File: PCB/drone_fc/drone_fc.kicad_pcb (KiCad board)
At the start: 4 copper layers, 1 part, among them U1 nRF52840

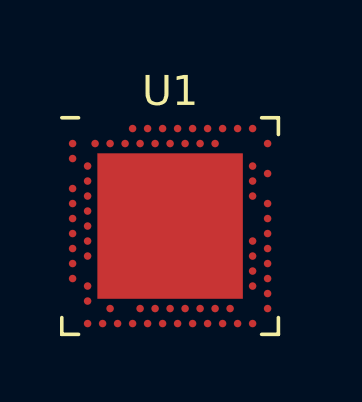
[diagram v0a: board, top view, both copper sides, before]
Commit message: Starting a PCB with the nRF52840. The Nordic-provided boards crash KiCAD so I'm making it myself I guess
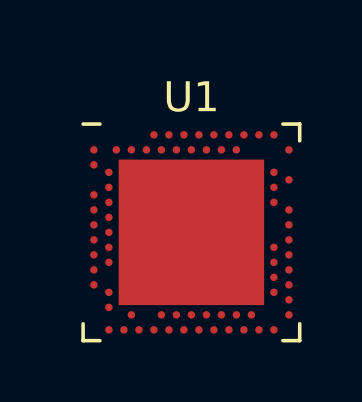
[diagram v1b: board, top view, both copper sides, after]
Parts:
- U1: footprint Package_DFN_QFN:Nordic_AQFN-73-1EP_7x7mm_P0.5mm -> nRF52840:nRF52840
- moved U1 0.74 mm to (53.3, 38.1)
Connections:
- U1 pad A22: Net-(U1-VDD-PadA22) -> unconnected-(U1-VDD-PadA22)
- U1 pad AD14: Net-(U1-VDD-PadA22) -> unconnected-(U1-VDD-PadAD14)
- U1 pad AD23: Net-(U1-VDD-PadA22) -> unconnected-(U1-VDD-PadAD23)
- U1 pad B1: Net-(U1-VDD-PadA22) -> VDD
- U1 pad B7: Net-(U1-VSS-PadB7) -> unconnected-(U1-VSS-PadB7)
- U1 pad W1: Net-(U1-VDD-PadA22) -> unconnected-(U1-VDD-PadW1)

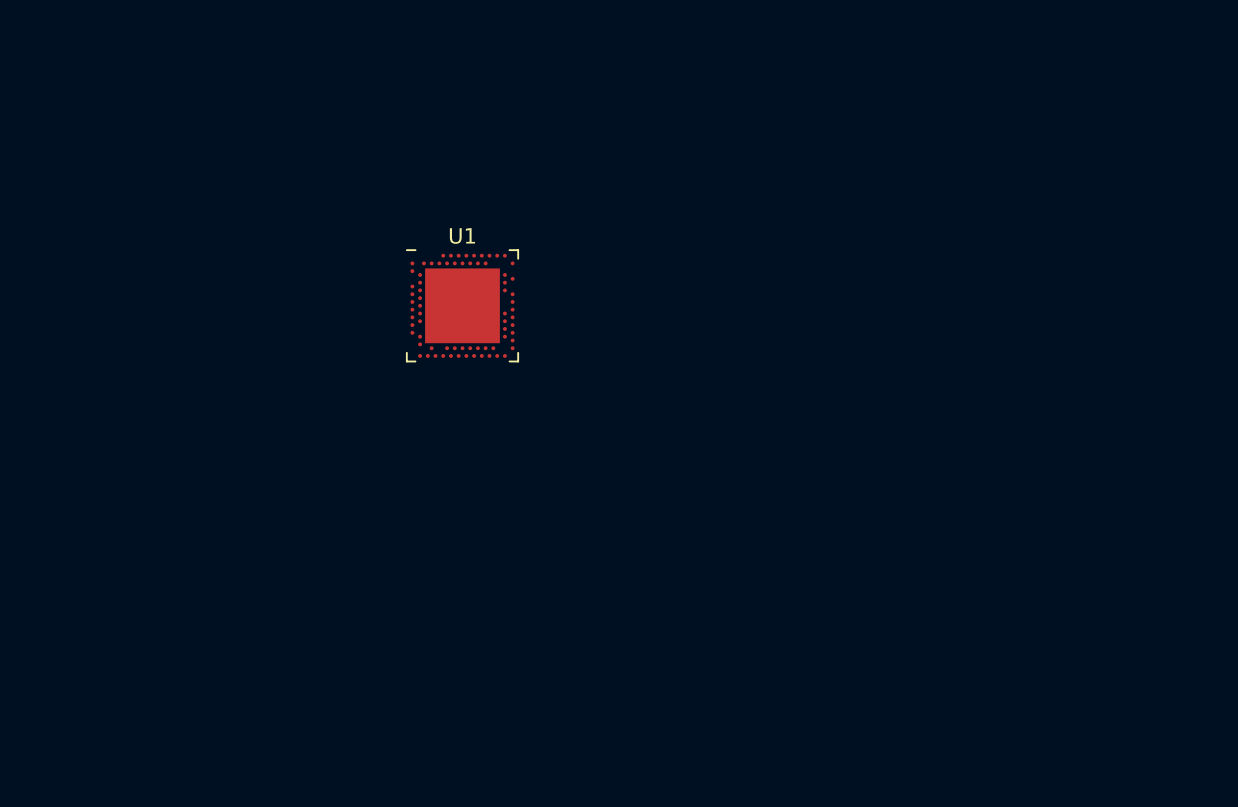
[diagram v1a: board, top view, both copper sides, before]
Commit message: Finished basic configuration schematic for nRF52840 and added USB receptacle and ESD protection
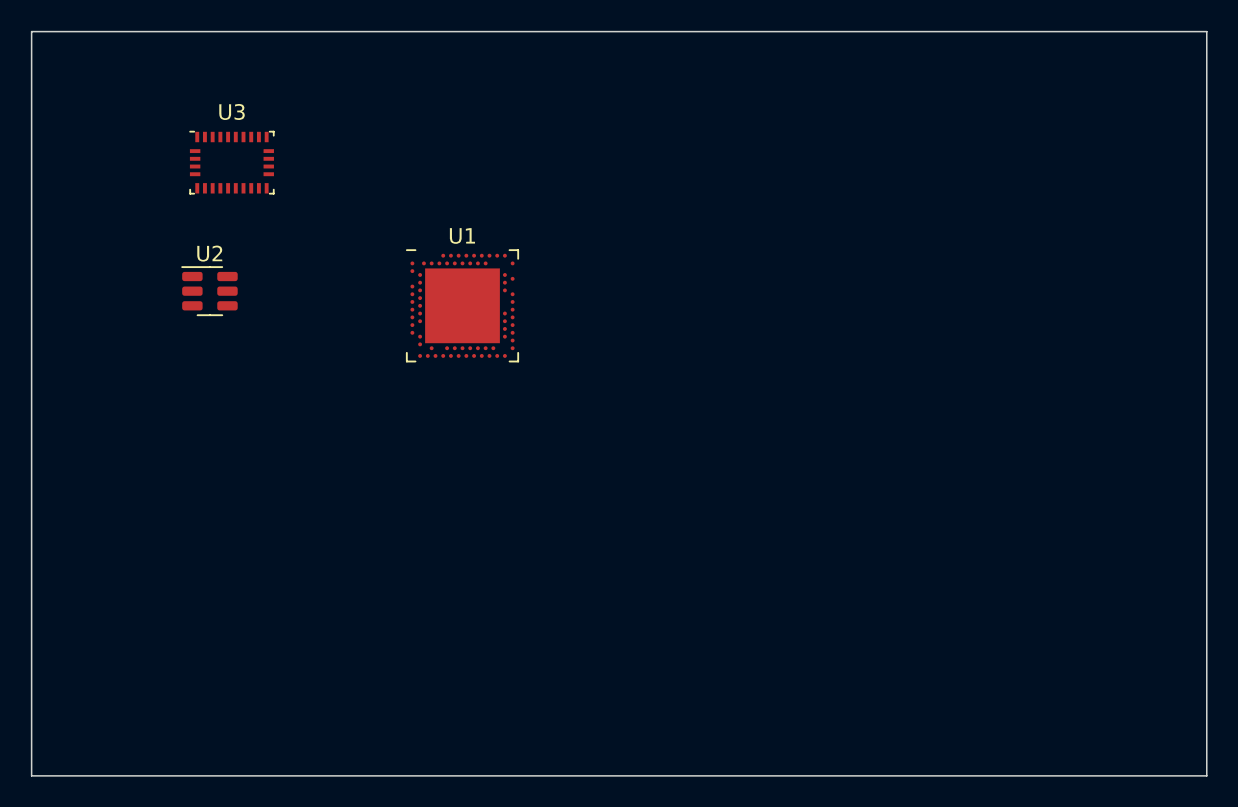
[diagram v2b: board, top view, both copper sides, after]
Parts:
- added U2: USBLC6-2SC6, Package_TO_SOT_SMD:SOT-23-6, F.Cu at (37.0, 37.1)
- added U3: BNO055, Package_LGA:LGA-28_5.2x3.8mm_P0.5mm, F.Cu at (38.4, 28.8)
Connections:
- U1 pad A18: unconnected-(U1-DEC2-PadA18) -> Net-(U1-DEC2)
- U1 pad A22: unconnected-(U1-VDD-PadA22) -> +15V
- U1 pad A23: unconnected-(U1-XC2-PadA23) -> Net-(U1-XC2)
- U1 pad AC5: unconnected-(U1-DECUSB-PadAC5) -> Net-(U1-DECUSB)
- U1 pad AD14: unconnected-(U1-VDD-PadAD14) -> +15V
- U1 pad AD2: unconnected-(U1-VBUS-PadAD2) -> VBUS
- U1 pad AD23: unconnected-(U1-VDD-PadAD23) -> +15V
- U1 pad AD4: unconnected-(U1-D--PadAD4) -> /D-
- U1 pad AD6: unconnected-(U1-D+-PadAD6) -> /D+
- U1 pad B1: VDD -> +15V
- U1 pad B24: unconnected-(U1-XC1-PadB24) -> Net-(U1-XC1)
- U1 pad B5: unconnected-(U1-DEC4-PadB5) -> /DEC4_6
- U1 pad B7: unconnected-(U1-VSS-PadB7) -> GND
- U1 pad C1: unconnected-(U1-DEC1-PadC1) -> /DEC1
- U1 pad D23: unconnected-(U1-DEC3-PadD23) -> /DEC3
- U1 pad E24: unconnected-(U1-DEC6-PadE24) -> /DEC4_6
- U1 pad F23: unconnected-(U1-VSS_PA-PadF23) -> GND
- U1 pad H23: unconnected-(U1-ANT-PadH23) -> Net-(U1-ANT)
- U1 pad W1: unconnected-(U1-VDD-PadW1) -> +15V
- U1 pad Y2: unconnected-(U1-VDDH-PadY2) -> VDDH
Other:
- board outline added: 76.2 x 48.3 mm

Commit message: Well the BNO055 isn't recommended for new projects, so I've replaced it with the ICM-20948, and updated the PCB's edge to hopefully match the ESC
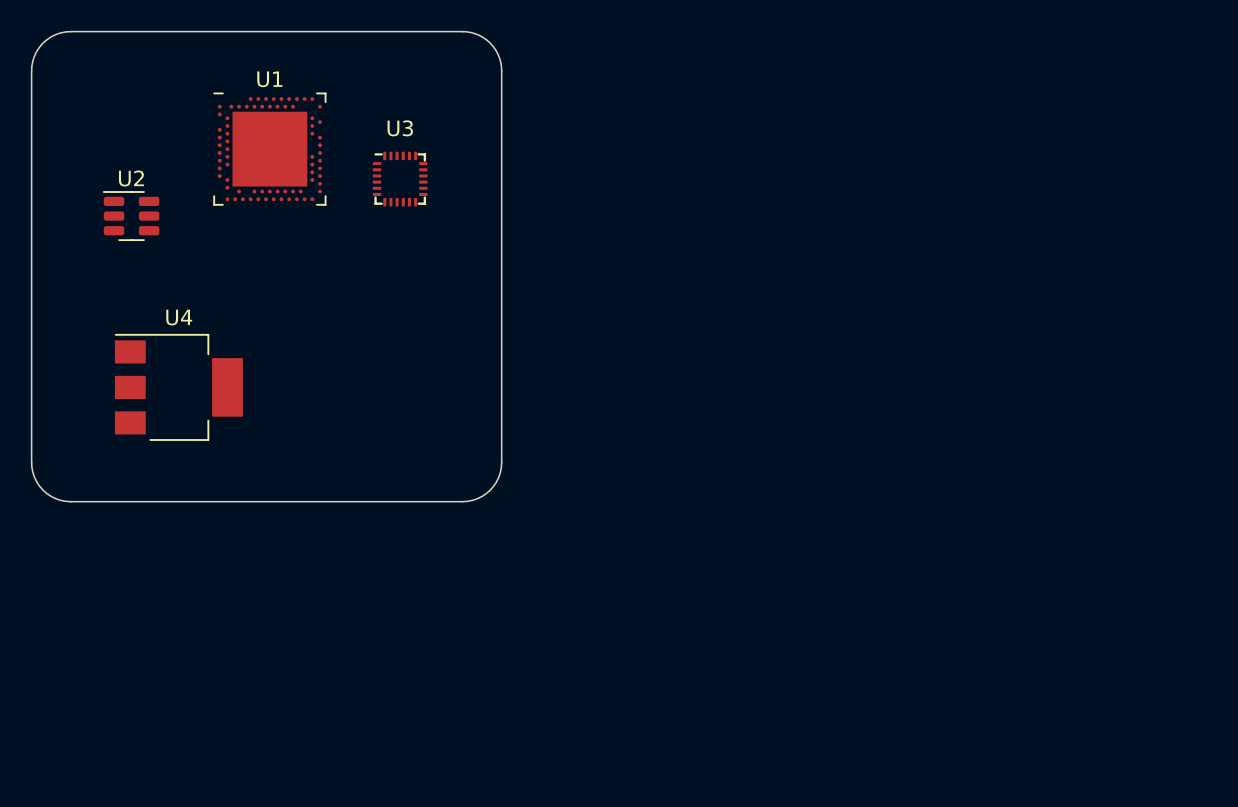
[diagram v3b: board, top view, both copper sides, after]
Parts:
- added U4: MCP1703AT-3302E/DB, Package_TO_SOT_SMD:SOT-223-3_TabPin2, F.Cu at (35.0, 43.4)
- U3: value BNO055 -> ICM-20948; footprint Package_LGA:LGA-28_5.2x3.8mm_P0.5mm -> Sensor_Motion:InvenSense_QFN-24_3x3mm_P0.4mm
- moved U1 16.1 mm to (40.9, 27.9)
- moved U3 11.0 mm to (49.3, 29.9)
- moved U2 7.04 mm to (31.9, 32.3)
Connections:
- U1 pad A22: +15V -> VDD
- U1 pad AD14: +15V -> VDD
- U1 pad AD23: +15V -> VDD
- U1 pad B1: +15V -> VDD
- U1 pad W1: +15V -> VDD
- U2 pad 5: +15V -> VDD
- U3 pad 10: unconnected-(U3-BL_IND-Pad10) -> Net-(U3-REGOUT)
- U3 pad 13: unconnected-(U3-PIN13-Pad13) -> VDD
- U3 pad 15: Net-(U3-GNDIO-Pad15) -> unconnected-(U3-NC-Pad15)
- U3 pad 16: Net-(U3-GNDIO-Pad15) -> unconnected-(U3-NC-Pad16)
- U3 pad 18: unconnected-(U3-COM2-Pad18) -> GND
- U3 pad 20: unconnected-(U3-COM0-Pad20) -> GND
- U3 pad 23: unconnected-(U3-PIN23-Pad23) -> /SCL
- U3 pad 24: unconnected-(U3-PIN24-Pad24) -> /SDA
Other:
- board size 76.2 x 48.3 mm -> 30.5 x 30.5 mm

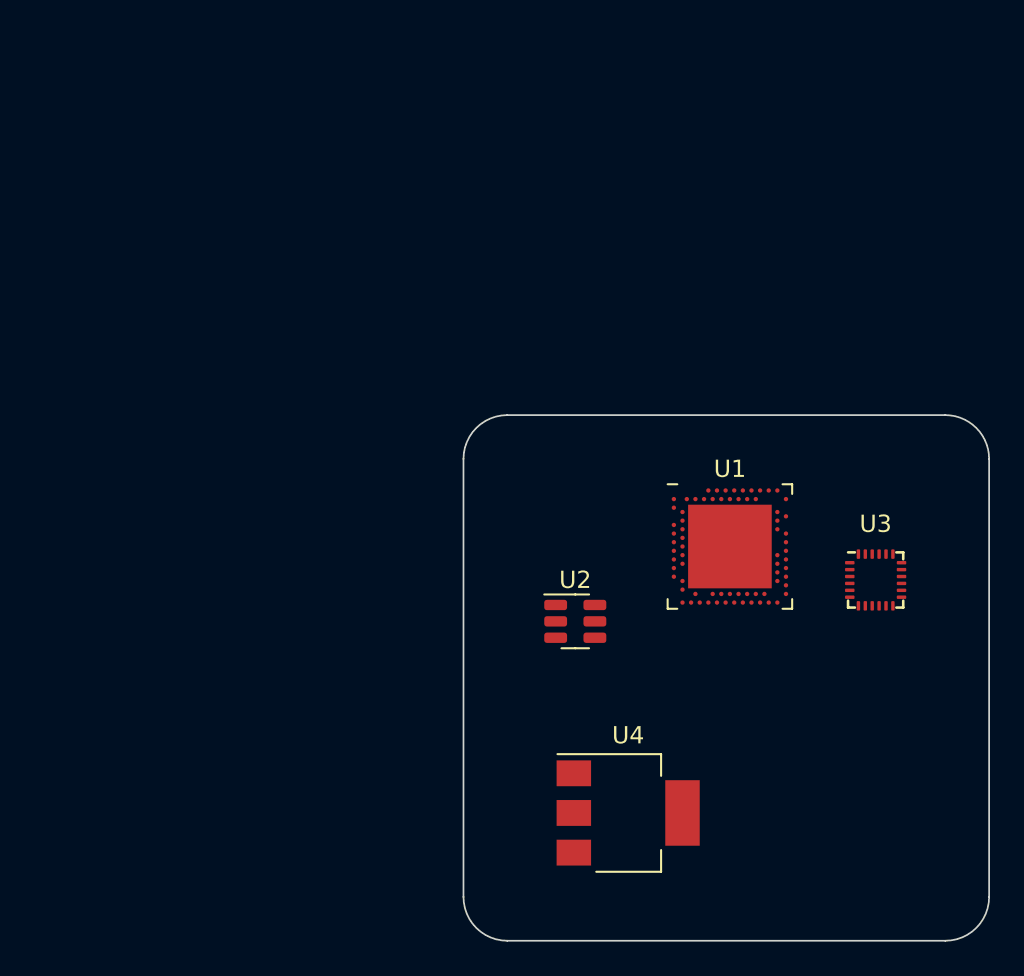
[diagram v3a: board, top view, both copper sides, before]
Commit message: Routed out the nRF52840 so I could tell which pins were best for peripherals
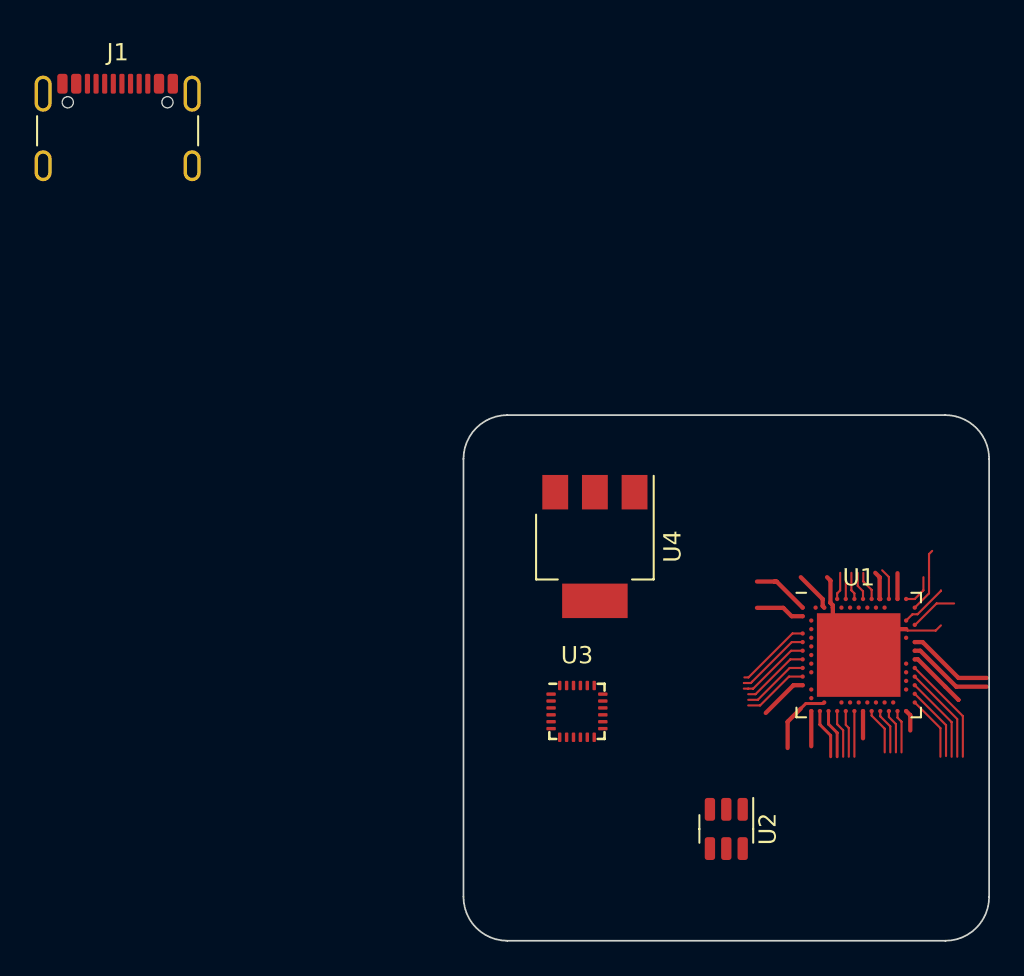
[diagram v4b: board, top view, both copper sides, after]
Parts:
- added J1: USB_C_Receptacle_USB2.0_16P, Connector_USB:USB_C_Receptacle_GCT_USB4105-xx-A_16P_TopMnt_Horizontal, F.Cu at (5.34, 4.79)
- moved U3 18.9 mm to (32.0, 37.5)
- moved U4 15.6 mm to (33.0, 27.9), turned to -90 degrees
- moved U2 14.9 mm to (40.6, 44.3), turned to -90 degrees
- moved U1 9.77 mm to (48.3, 34.2)
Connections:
- U1 pad Y2: VDDH -> VBUS
- U3 pad 11: unconnected-(U3-FSYNC-Pad11) -> GND
- U3 pad 12: unconnected-(U3-INT1-Pad12) -> /IMU_INT
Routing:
- net GND: track 0.00 -> 10.8 mm
- net VDD: track 0.00 -> 10.4 mm
- net unconnected-(U1-P1.06-PadR24): track 0.00 -> 6.30 mm
- net unconnected-(U1-P1.04-PadU24): track 0.00 -> 5.67 mm
- net /DEC4_6: track 0.00 -> 5.12 mm
- net unconnected-(U1-NFC1/P0.09-PadL24): track 0.00 -> 5.05 mm
- net unconnected-(U1-NFC2/P0.10-PadJ24): track 0.00 -> 5.05 mm
- net unconnected-(U1-P1.02-PadW24): track 0.00 -> 5.04 mm
- net unconnected-(U1-P0.26-PadG1): track 0.00 -> 4.44 mm
- net unconnected-(U1-AIN2/P0.04-PadJ1): track 0.00 -> 4.39 mm
- net unconnected-(U1-SWDCLK-PadAA24): track 0.00 -> 4.36 mm
- net unconnected-(U1-P0.06-PadL1): track 0.00 -> 4.32 mm
- net Net-(U1-DECUSB): track 0.00 -> 4.11 mm
- net unconnected-(U1-P0.08-PadN1): track 0.00 -> 4.00 mm
- net unconnected-(U1-TRACEDATA3/P1.09-PadR1): track 0.00 -> 3.92 mm
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
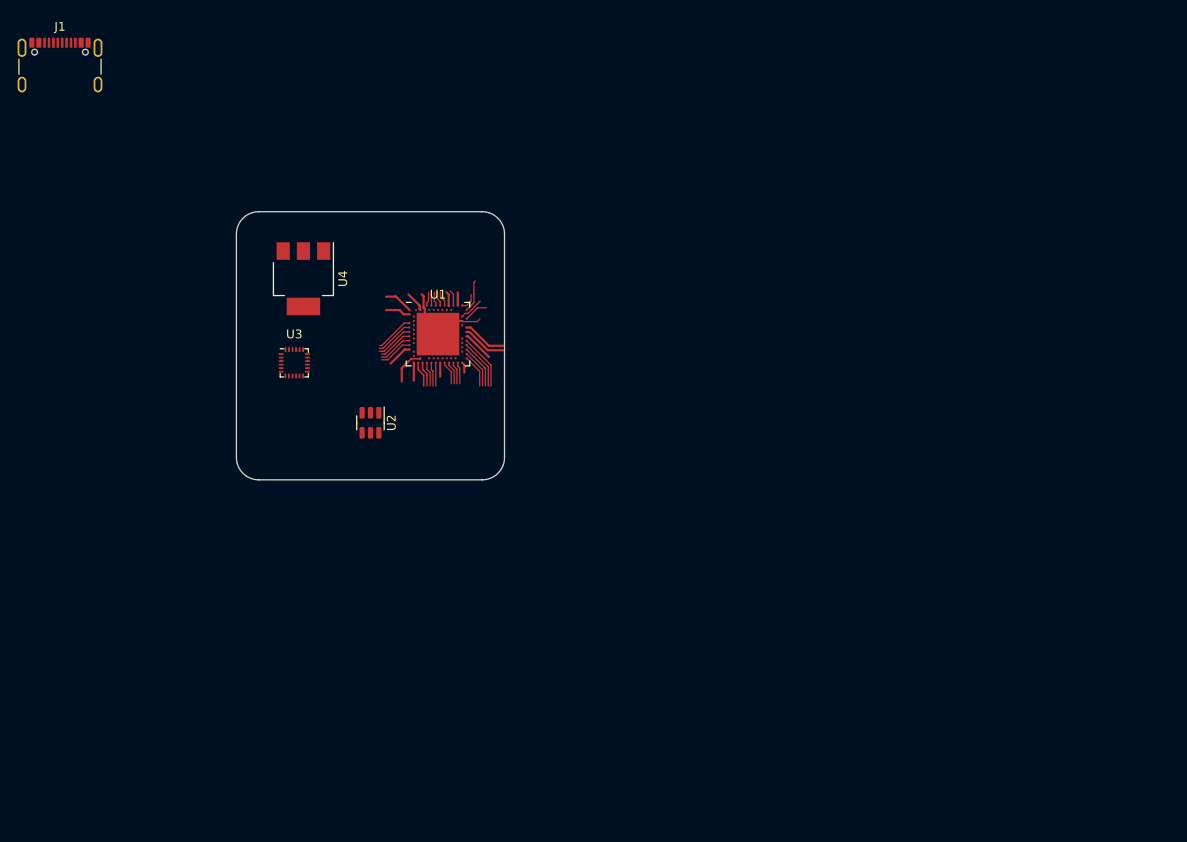
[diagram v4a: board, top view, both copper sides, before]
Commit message: Adjusted PCB size to more accurately match the ESC and added MOSFETs to provide logic level shifting on the I2C lines between the uC and IMU (thanks Adafruit and Digikey)
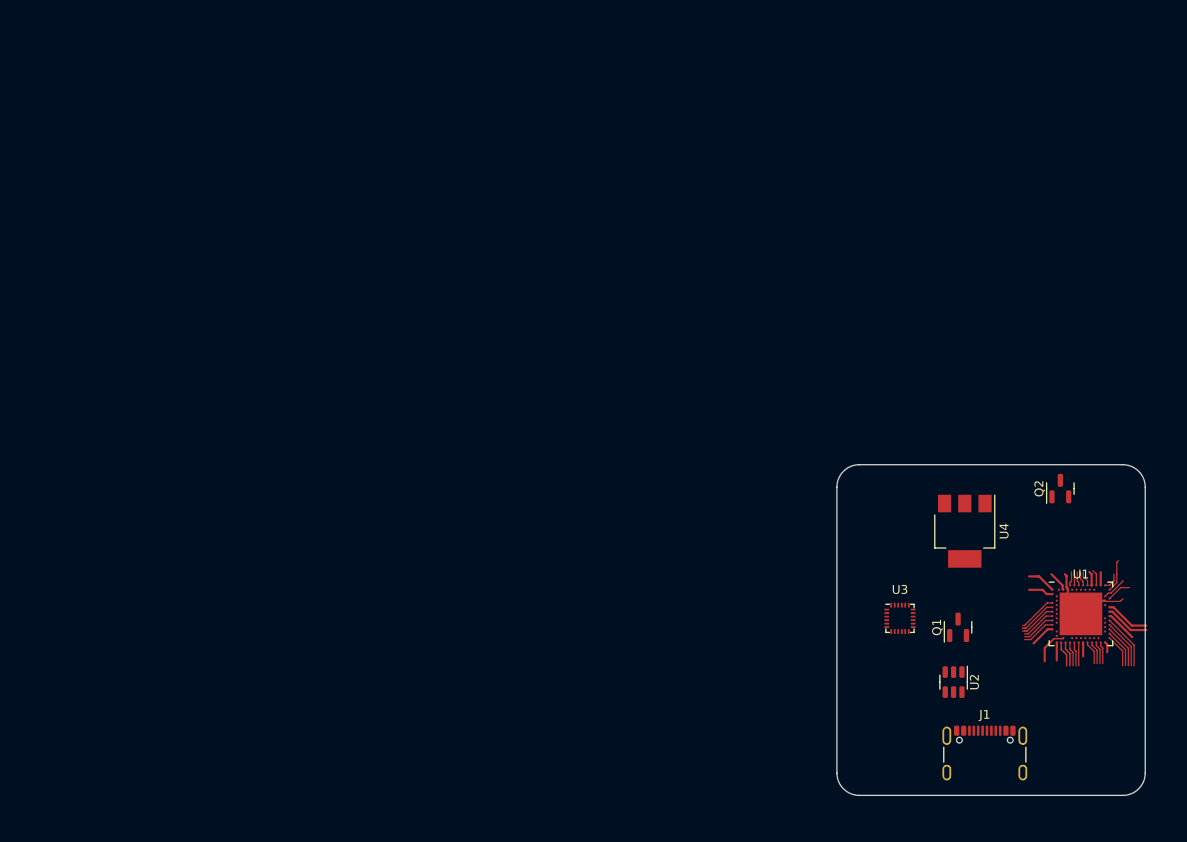
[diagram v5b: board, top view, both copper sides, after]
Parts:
- added Q1: BSS138, Package_TO_SOT_SMD:SOT-23, F.Cu at (107.4, 67.6)
- added Q2: BSS138, Package_TO_SOT_SMD:SOT-23, F.Cu at (119.1, 51.8)
- moved J1 131.0 mm to (110.5, 83.0)
- moved U4 80.5 mm to (108.2, 56.6)
- moved U1 79.7 mm to (121.4, 66.0)
- moved U3 74.7 mm to (100.8, 66.5)
- moved U2 72.6 mm to (106.9, 73.8)
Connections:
- U3 pad 13: VDD -> Net-(Q1-G)
- U3 pad 23: /SCL -> /SCL_1_8
- U3 pad 24: /SDA -> /SDA_1_8
- U3 pad 8: unconnected-(U3-VDDIO-Pad8) -> Net-(Q1-G)
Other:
- board size 30.5 x 30.5 mm -> 35.1 x 37.6 mm
